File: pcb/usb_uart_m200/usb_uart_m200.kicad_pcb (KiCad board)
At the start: 2 copper layers, 22 parts, among them J1 Conn_01x02_Socket, J4 USB_A, J6 Conn_01x08_Pin, P1 USB_C_Plug_USB2.0, P2 USB_C_Plug_USB2.0, U1 CY7C65213-28PVXI, U2 TC1015-xCT, U4 USBLC6-2SC6

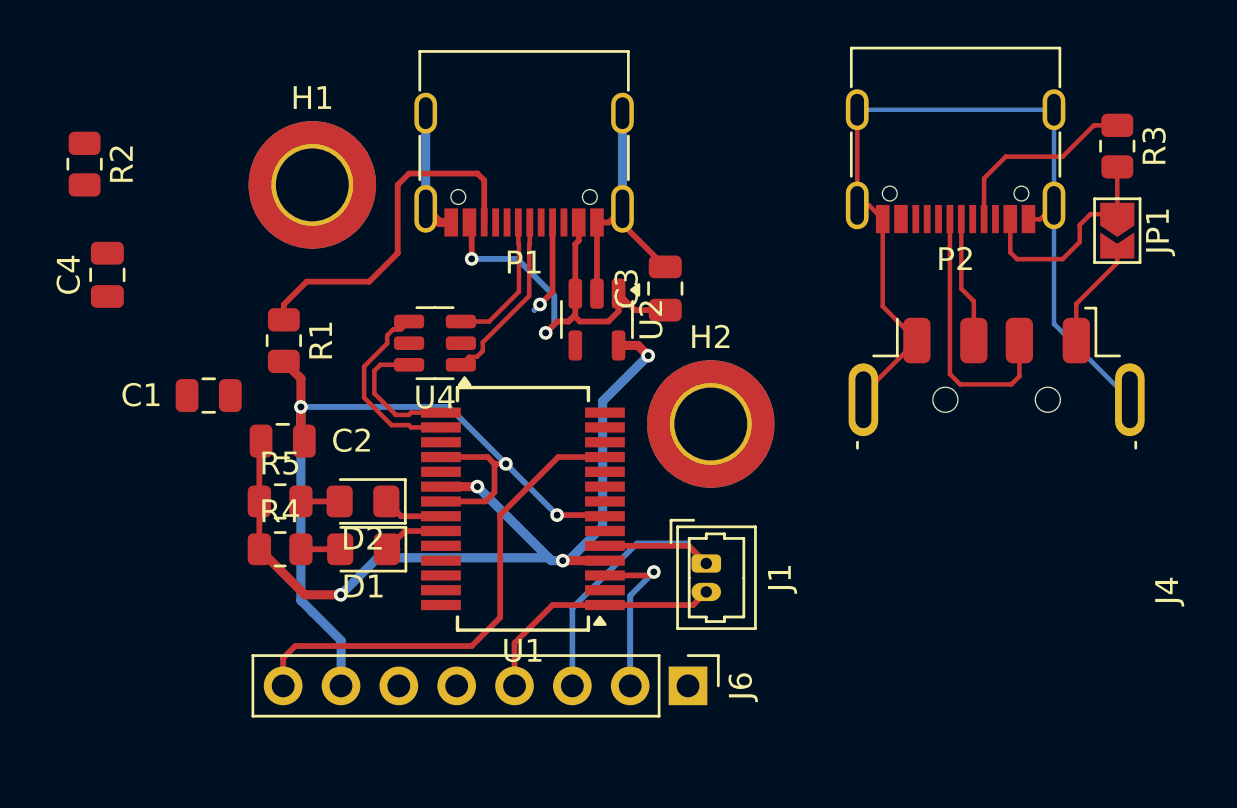
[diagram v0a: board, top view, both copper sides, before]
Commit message: Routing
Separated the uart from the FEL adapter board.
Adds a led wire connector for the ground pin.
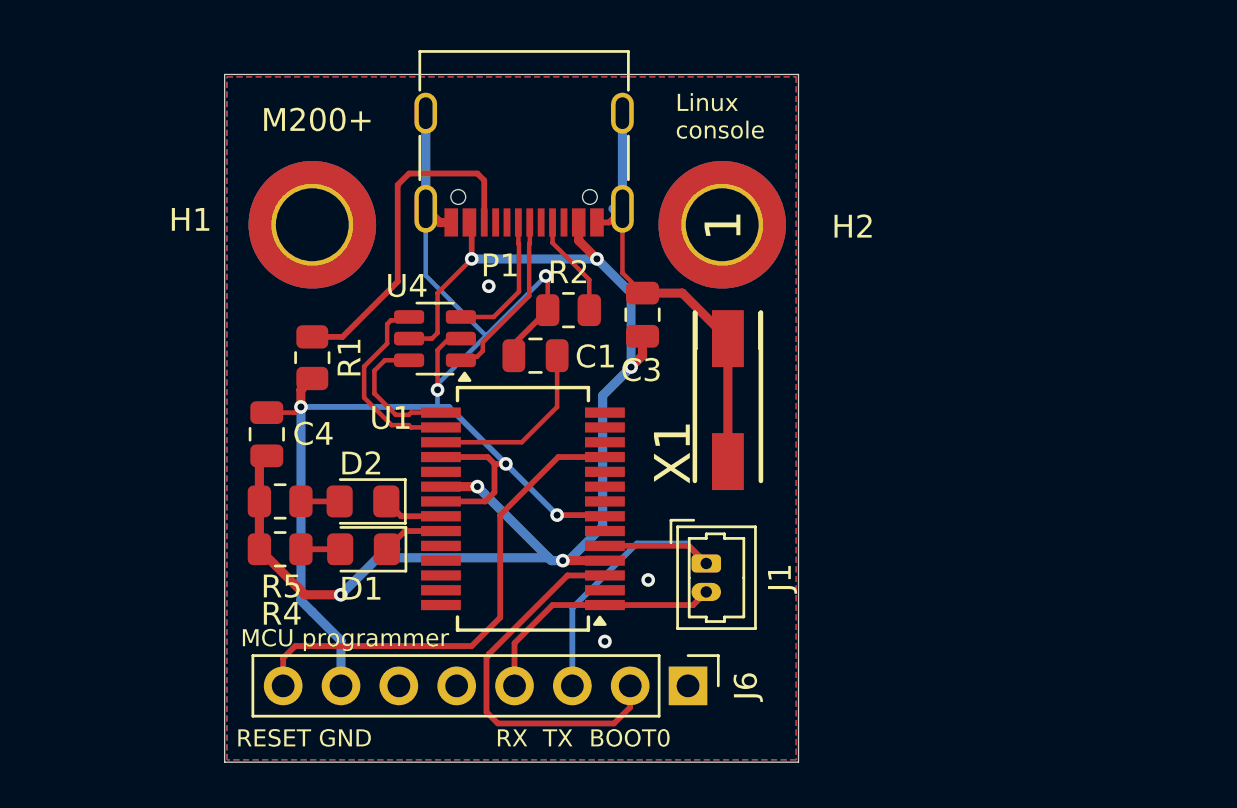
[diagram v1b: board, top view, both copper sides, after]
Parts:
- removed C2: 1µF, Capacitor_SMD:C_0805_2012Metric
- removed J4: USB_A, Connector_USB:USB_A_Molex_48037-2200_Horizontal
- removed JP1: SolderJumper_2_Open, Jumper:SolderJumper-2_P1.3mm_Open_TrianglePad1.0x1.5mm
- removed P2: USB_C_Plug_USB2.0, Connector_USB:USB_C_Receptacle_G-Switch_GT-USB-7010ASV
- removed R3: 5.1k, Resistor_SMD:R_0805_2012Metric
- removed U2: TC1015-xCT, Package_TO_SOT_SMD:SOT-23-5
- added X1: 2059-301_998-403, 2059-301_998-403:P-2059-301_998-403, F.Cu at (169.0, 68.3)
- C3: value 1µF -> 1µF10V
- moved R2 22.2 mm to (162.0, 64.2), turned to 180 degrees
- moved C1 14.5 mm to (160.6, 66.2)
- moved C4 9.90 mm to (148.8, 69.7)
- moved H2 8.76 mm to (168.8, 60.5)
- moved H1 1.75 mm to (150.8, 60.5)
- moved C3 1.52 mm to (165.2, 64.5)
- moved R1 1.46 mm to (150.8, 66.3)
- moved U4 0.20 mm to (156.1, 65.5)
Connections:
- C3 pad 1: /VBUS -> /3v3
- C4 pad 1: /VBUS -> /3v3
- J6 pad 1: /3V3 -> unconnected-(J6-Pin_1-Pad1)
- P1 pad A4: /VBUS -> /3v3
- P1 pad A9: /VBUS -> /3v3
- P1 pad B4: /VBUS -> /3v3
- P1 pad B9: /VBUS -> /3v3
- U4 pad 5: /VBUS -> /3v3
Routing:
- net /ALTER_GND: track 39.2 -> 0.00 mm
- net GND: track 56.5 -> 85.9 mm, vias 3 -> 8
- net /VBUS: track 18.8 -> 0.00 mm, vias 2 -> 0
- net /3v3: track 40.2 -> 58.3 mm, vias 4 -> 6
- net Net-(J4-D-): track 11.8 -> 0.00 mm
- net Net-(JP1-A): track 9.62 -> 0.00 mm
- net /BOOT0: track 7.64 -> 16.9 mm, vias 1 -> 0
- net Net-(P2-CC): track 8.60 -> 0.00 mm
- net Net-(U1-VCCD): track 0.07 -> 8.06 mm
- net Net-(J4-D+): track 5.56 -> 0.00 mm
- net Net-(J4-VBUS): track 4.85 -> 0.00 mm
- net Net-(P1-VCONN): track 15.6 -> 15.0 mm
- net Net-(P1-CC): track 4.18 -> 4.52 mm, vias 1 -> 0
- added copper zone on B.Cu, net GND
- added copper zone on F.Cu, net GND
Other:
- board outline added: 25.2 x 30.2 mm
- board text added: "BOOT0"
- board text added: "Linux console"
- board text added: "M200+"
- board text added: "MCU programmer"
- board text added: "RESET GND"
- board text added: "RX TX"

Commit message: Fix the board: add a regulator and farnelle references. Add a pull up on boot0
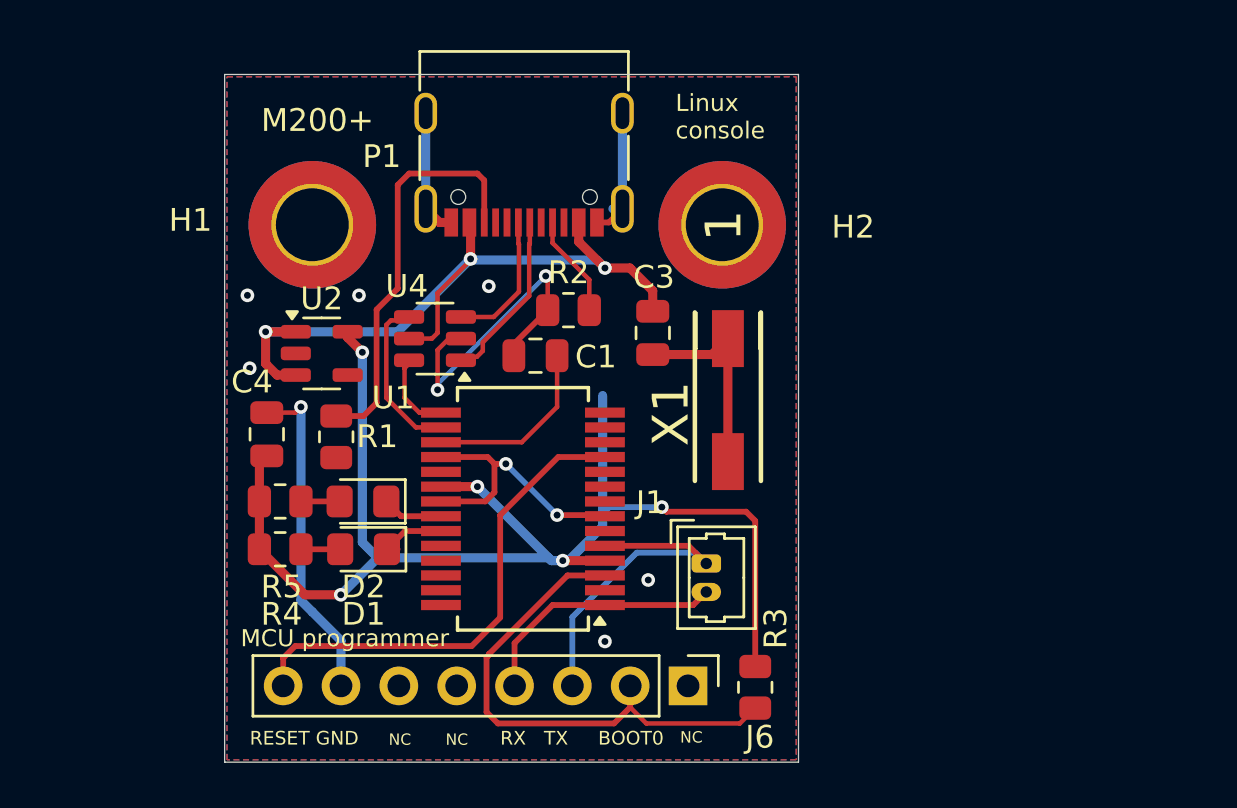
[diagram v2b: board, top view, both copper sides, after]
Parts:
- added R3: 10k, Resistor_SMD:R_0805_2012Metric, F.Cu at (170.2, 80.8)
- added U2: MIC5317-3.3xM5, Package_TO_SOT_SMD:SOT-23-5, F.Cu at (151.2, 66.2)
- R1, R2: value 5.1k -> 22k
- moved R1 3.63 mm to (151.8, 69.8)
- moved C3 0.92 mm to (165.7, 65.2), turned to -90 degrees
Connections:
- C3 pad 1: /3v3 -> /VBUS
- P1 pad A4: /3v3 -> /VBUS
- P1 pad A9: /3v3 -> /VBUS
- P1 pad B4: /3v3 -> /VBUS
- P1 pad B9: /3v3 -> /VBUS
- U4 pad 5: /3v3 -> /VBUS
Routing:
- net /VBUS: track 0.00 -> 33.5 mm, vias 0 -> 3
- net GND: track 85.9 -> 61.9 mm, vias 8 -> 11
- net /BOOT0: track 16.9 -> 22.9 mm
- net Net-(P1-VCONN): track 15.0 -> 18.0 mm
- net /D_ESDP: track 6.07 -> 3.60 mm
- net /D_ESDN: track 8.66 -> 7.28 mm
- net /3v3: track 58.3 -> 59.2 mm, vias 6 -> 5
- net /MCU/CON_TX_PC_RX: track 15.6 -> 15.0 mm
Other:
- board text added: "NC"

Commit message: Fix on the usb uart power, it uses vbus.
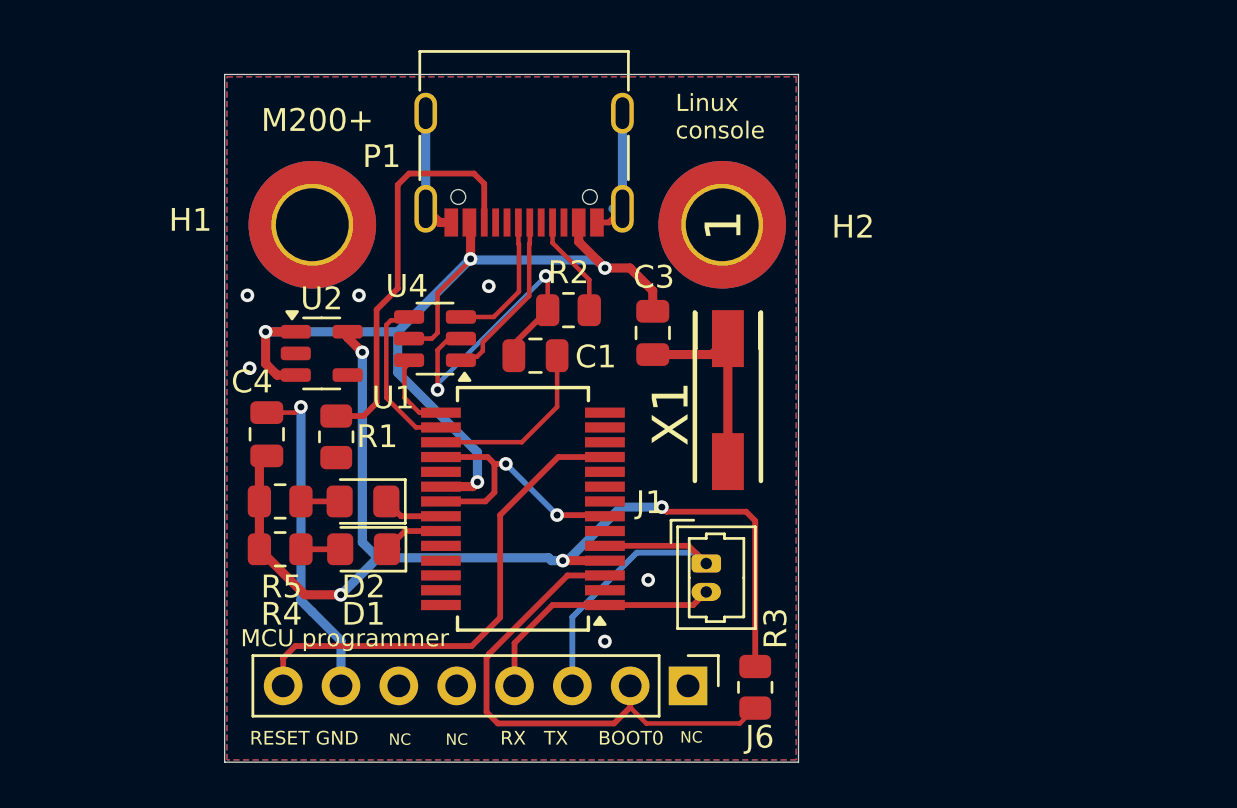
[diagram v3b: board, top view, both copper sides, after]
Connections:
- U1 pad 20: /3v3 -> /VBUS
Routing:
- net /3v3: track 59.2 -> 47.5 mm, vias 5 -> 4
- net /VBUS: track 33.5 -> 43.2 mm, vias 3 -> 4
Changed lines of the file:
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@@
 			)
 		)
+		(property "farnell" "3729173"
+			(at 0 0 -90)
+			(unlocked yes)
+			(layer "F.Fab")
+			(hide yes)
+			(effects
+				(font
+					(size 1 1)
+					(thickness 0.15)
+				)
+			)
+		)
 		(property ki_fp_filters "Connector*:*_1x??_*")
 		(sheetname "Root")
@@
 			)
 		)
+		(property "farnell" "9733051"
+			(at 0 0 -90)
+			(unlocked yes)
+			(layer "F.Fab")
+			(hide yes)
+			(effects
+				(font
+					(size 1 1)
+					(thickness 0.15)
+				)
+			)
+		)
 		(property ki_fp_filters "Connector*:*_1x??_*")
 		(sheetname "Root")
@@
 			(size 1.75 0.45)
 			(layers "F.Cu" "F.Paste" "F.Mask")
-			(net 3 "/3v3")
+			(net 35 "/VBUS")
 			(pinfunction "VCC")
 			(pintype "power_in")
@@
 	)
 	(segment
-		(start 158 72)
-		(end 156.4 72)
-		(width 0.4)
-		(layer "F.Cu")
-		(net 3)
-	)
-	(segment
 		(start 150.425 76.75)
 		(end 148.425 74.75)
@@
 	)
 	(via
-		(at 158 72)
-		(size 0.6)
-		(drill 0.3)
-		(layers "F.Cu" "B.Cu")
-		(net 3)
-	)
-	(via
 		(at 161.75 75.25)
 		(size 0.6)
@@
 	)
 	(segment
-		(start 166.1 72.9)
-		(end 163.8 72.9)
-		(width 0.254)
-		(layer "B.Cu")
-		(net 3)
-	)
-	(segment
-		(start 163.5 73.75)
-		(end 162 75.25)
+		(start 164.3 72.9)
+		(end 161.95 75.25)
 		(width 0.4)
 		(layer "B.Cu")
@@
 	)
 	(segment
-		(start 163.8 72.9)
-		(end 163.5 73.2)
-		(width 0.254)
-		(layer "B.Cu")
-		(net 3)
-	)
-	(segment
-		(start 163.5 68)
-		(end 163.5 73.2)
-		(width 0.4)
-		(layer "B.Cu")
-		(net 3)
-	)
-	(segment
 		(start 161.75 75.25)
 		(end 161.25 75.25)
@@
 	)
 	(segment
-		(start 163.5 73.2)
-		(end 163.5 73.75)
+		(start 152.946 66.1)
+		(end 152.946 74.446)
 		(width 0.4)
 		(layer "B.Cu")
@@
 	)
 	(segment
-		(start 152.946 66.1)
-		(end 152.946 74.446)
+		(start 161.95 75.25)
+		(end 161.75 75.25)
 		(width 0.4)
 		(layer "B.Cu")
@@
 	)
 	(segment
-		(start 161.125 75.125)
-		(end 161.25 75.25)
-		(width 0.4)
-		(layer "B.Cu")
-		(net 3)
-	)
-	(segment
-		(start 162 75.25)
-		(end 161.75 75.25)
+		(start 166.1 72.9)
+		(end 164.3 72.9)
 		(width 0.4)
 		(layer "B.Cu")
@@
 	)
 	(segment
-		(start 161.25 75.25)
-		(end 158 72)
+		(start 161.125 75.125)
+		(end 161.25 75.25)
 		(width 0.4)
 		(layer "B.Cu")
@@
 	)
 	(segment
-		(start 154.5 63.3)
-		(end 153.573 64.227)
+		(start 154.5 58.75)
+		(end 154.5 63.3)
 		(width 0.254)
 		(layer "F.Cu")
@@
 	)
 	(segment
-		(start 153.573 68.327)
-		(end 153 68.9)
+		(start 157.85 58.25)
+		(end 155 58.25)
 		(width 0.254)
 		(layer "F.Cu")
@@
 	)
 	(segment
-		(start 154.5 58.75)
-		(end 154.5 63.3)
+		(start 153.573 64.227)
+		(end 153.573 68.327)
 		(width 0.254)
 		(layer "F.Cu")
@@
 	)
 	(segment
-		(start 158 58.25)
-		(end 155 58.25)
+		(start 153.573 68.327)
+		(end 153 68.9)
 		(width 0.254)
 		(layer "F.Cu")
@@
 	)
 	(segment
-		(start 155 58.25)
-		(end 154.5 58.75)
+		(start 158.3 60.4)
+		(end 158.3 58.7)
 		(width 0.254)
 		(layer "F.Cu")
@@
 	)
 	(segment
-		(start 153 68.9)
-		(end 151.8 68.9)
+		(start 158.3 58.7)
+		(end 157.85 58.25)
 		(width 0.254)
 		(layer "F.Cu")
@@
 	)
 	(segment
-		(start 158.3 58.55)
-		(end 158 58.25)
+		(start 153 68.9)
+		(end 151.8 68.9)
 		(width 0.254)
 		(layer "F.Cu")
@@
 	)
 	(segment
-		(start 153.573 64.227)
-		(end 153.573 68.327)
+		(start 154.5 63.3)
+		(end 153.573 64.227)
 		(width 0.254)
 		(layer "F.Cu")
@@
 	)
 	(segment
-		(start 158.3 60.4)
-		(end 158.3 58.55)
+		(start 155 58.25)
+		(end 154.5 58.75)
 		(width 0.254)
 		(layer "F.Cu")
@@
 	)
 	(segment
+		(start 156.4 72)
+		(end 157.8 72)
+		(width 0.4)
+		(layer "F.Cu")
+		(net 35)
+	)
+	(segment
 		(start 155 65.5)
 		(end 156 65.5)
@@
 	)
 	(segment
+		(start 157.8 72)
+		(end 158 71.8)
+		(width 0.4)
+		(layer "F.Cu")
+		(net 35)
+	)
+	(segment
 		(start 148.7 65.2)
 		(end 150.025 65.2)
@@
 	)
 	(via
+		(at 158 71.8)
+		(size 0.6)
+		(drill 0.3)
+		(layers "F.Cu" "B.Cu")
+		(net 35)
+	)
+	(via
 		(at 148.7 65.2)
 		(size 0.6)
@@
 	)
 	(segment
+		(start 158 71.8)
+		(end 158 70.48995)
+		(width 0.4)
+		(layer "B.Cu")
+		(net 35)
+	)
+	(segment
 		(start 163.25 62.05)
 		(end 157.75 62.05)
@@
 	)
 	(segment
+		(start 154.5 66.98995)
+		(end 154.5 65.2)
+		(width 0.4)
+		(layer "B.Cu")
+		(net 35)
+	)
+	(segment
 		(start 157.75 62.05)
 		(end 157.7 62)
 		(width 0.4)
 		(layer "B.Cu")
+		(net 35)
+	)
+	(segment
+		(start 158 70.48995)
+		(end 154.5 66.98995)
+		(width 0.4)
+		(layer "B.Cu")

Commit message: Removed the DEBUG header from the serial port board since the MCU needs a stlink total erase.
Adds the screen capture of the configuration in Katapult menuconfig.
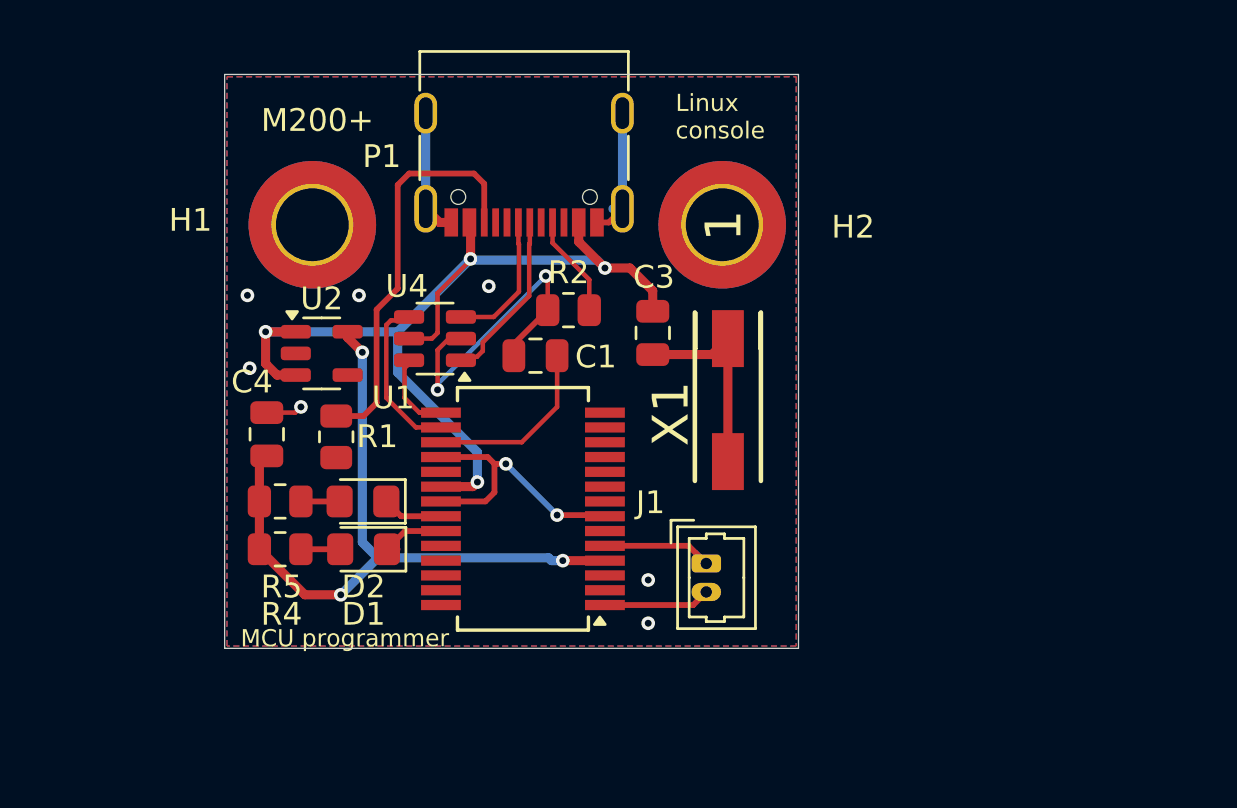
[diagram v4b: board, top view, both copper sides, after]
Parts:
- removed J6: Conn_01x08_Pin, Connector_PinHeader_2.54mm:PinHeader_1x08_P2.54mm_Vertical
- removed R3: 10k, Resistor_SMD:R_0805_2012Metric
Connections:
- U1 pad 11: /RESET -> unconnected-(U1-CTS-Pad11)
- U1 pad 3: /BOOT0 -> unconnected-(U1-RTS-Pad3)
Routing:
- net /BOOT0: track 22.9 -> 0.00 mm
- net /RESET: track 21.6 -> 0.00 mm
- net /3v3: track 47.5 -> 31.6 mm, vias 4 -> 3
- net GND: track 61.9 -> 49.0 mm
- net /MCU/CON_TX_PC_RX: track 15.0 -> 5.44 mm
- net /MCU/CON_RX_PC_TX: track 11.2 -> 4.69 mm
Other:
- board size 25.2 x 30.2 mm -> 25.2 x 25.2 mm
- board text removed: "BOOT0"
- board text removed: "NC"
- board text removed: "RESET GND"
- board text removed: "RX TX"

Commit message: PCB sources after production
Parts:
- H1, H2: footprint MountingHole:MountingHole_3.2mm_M3_DIN965_Pad_TopBottom -> MountingHole:MountingHole_2.2mm_M2_ISO7380
- moved H2 17.6 mm to (151.5, 57.2)
- moved H1 17.2 mm to (167.6, 57.3)
- moved R5 4.14 mm to (152.8, 70.4)
- moved R4 4.03 mm to (152.8, 76.8), turned to 180 degrees
- moved U2 3.56 mm to (151.4, 62.6)
- moved C4 2.87 mm to (150.6, 67.5)
- moved R1 2.48 mm to (152.7, 67.5)
- moved X1 2.46 mm to (166.6, 68.8), turned to -90 degrees
- moved C3 1.75 mm to (165.7, 63.5), turned to 0 degrees
- moved J1 1.36 mm to (166.7, 75.2)
- moved P1 0.41 mm to (159.7, 56.5)
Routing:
- net GND: track 49.0 -> 38.7 mm, vias 11 -> 15
- net /3v3: track 31.6 -> 39.2 mm, vias 3 -> 4
- net Net-(P1-VCONN): track 17.9 -> 14.2 mm
- net /VBUS: track 43.2 -> 46.3 mm, vias 4 -> 5
- net /MCU/CON_TX_PC_RX: track 5.44 -> 3.35 mm
- net Net-(D2-A): track 1.70 -> 2.99 mm
- net /MCU/CON_RX_PC_TX: track 4.69 -> 3.41 mm
- net Net-(D1-A): track 1.72 -> 2.35 mm
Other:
- board size 25.2 x 25.2 mm -> 25 x 25.1 mm
- board text added: "M200+ Linux console"
- board text removed: "Linux console"
- board text removed: "M200+"
- board text removed: "MCU programmer"
